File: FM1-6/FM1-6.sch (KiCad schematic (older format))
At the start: 13 parts

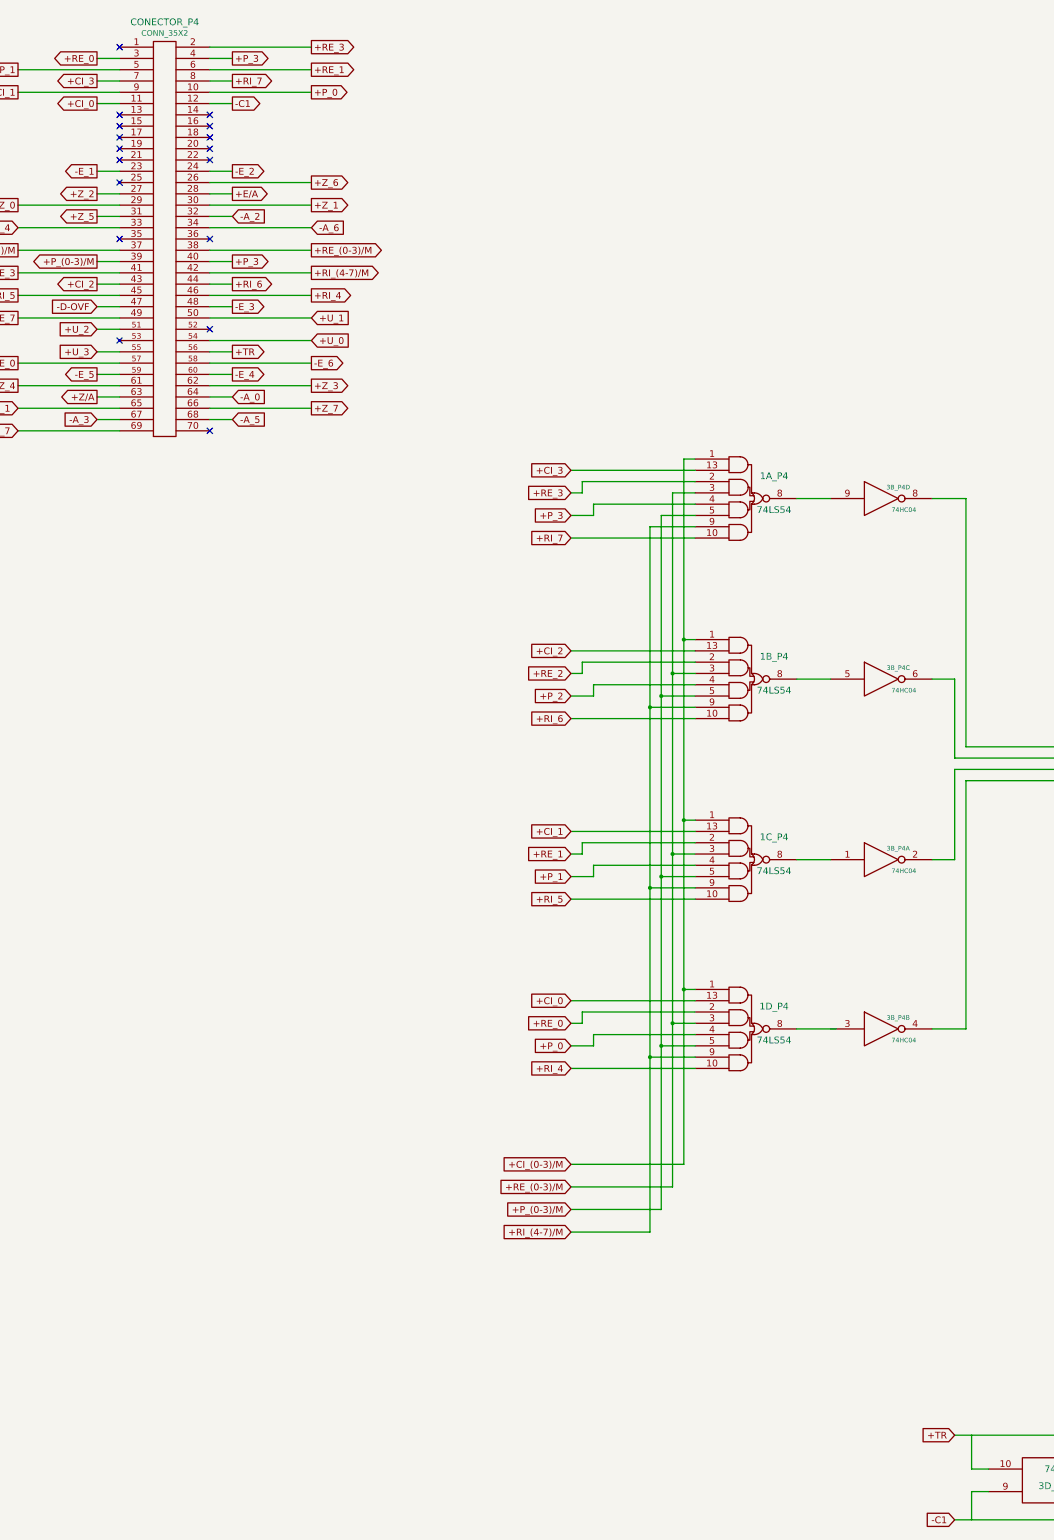
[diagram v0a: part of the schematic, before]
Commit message: criando novos projetos individuais para todas as outras pranchas que ainda faltavam serem migradas.
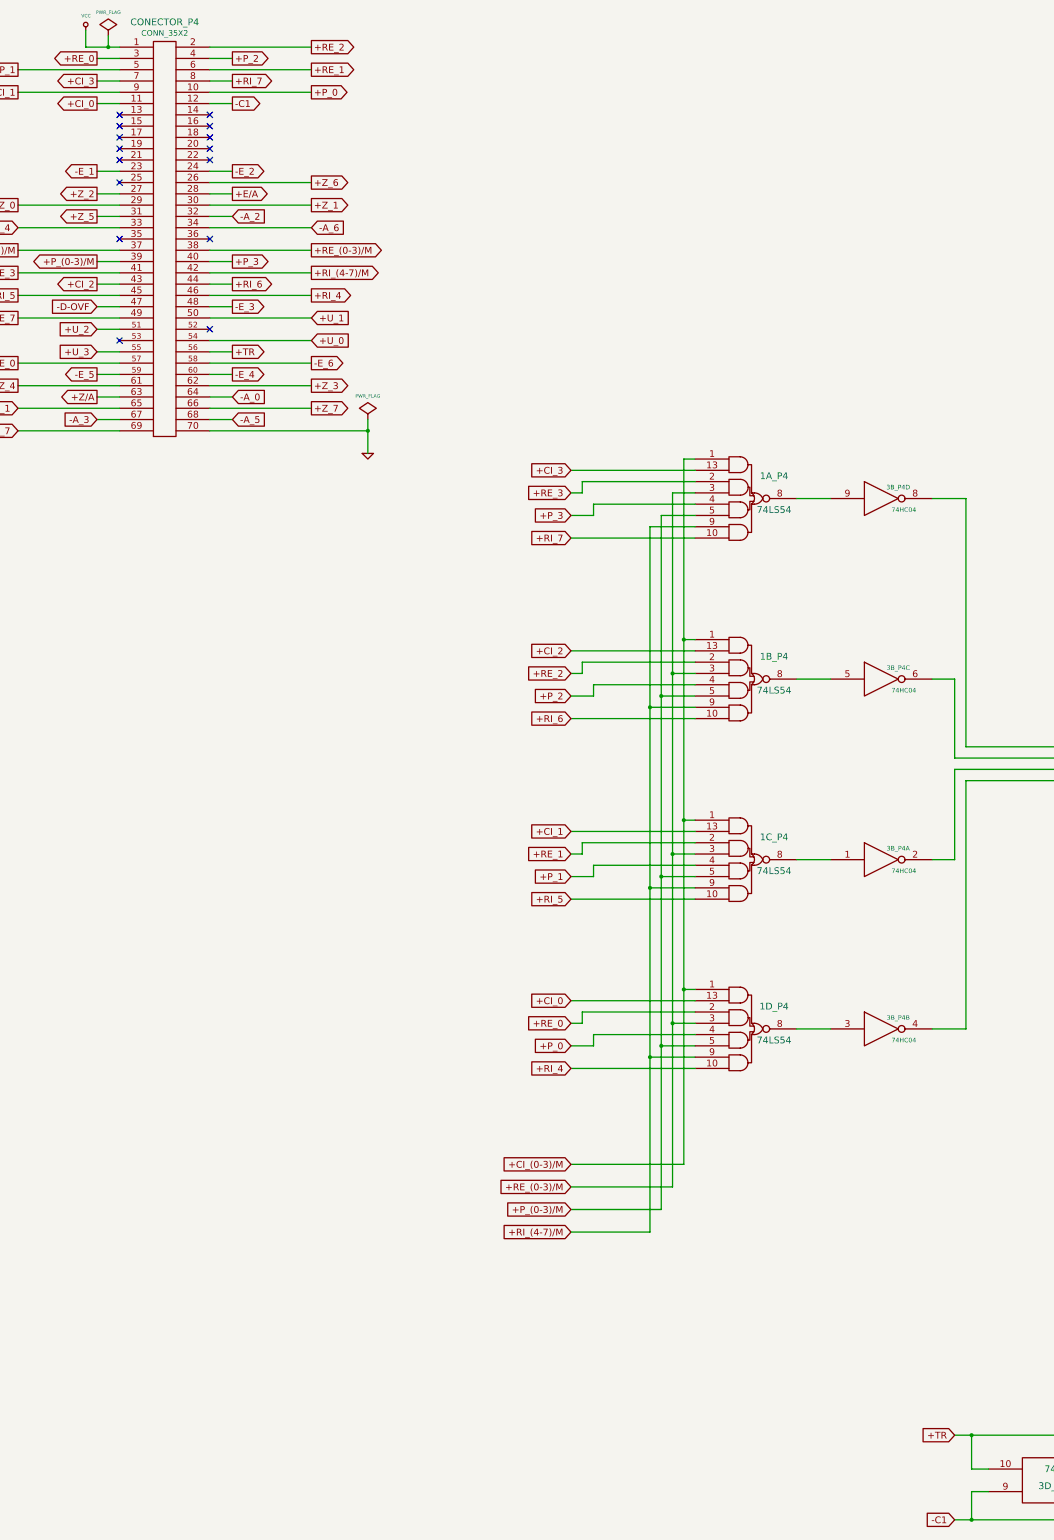
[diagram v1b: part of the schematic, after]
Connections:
- net +P_2: now also CONECTOR_P4.4 (P4)
- net +P_3: no longer CONECTOR_P4.4 (P4)
- net +RE_2: now also CONECTOR_P4.2 (P2)
- net +RE_3: no longer CONECTOR_P4.2 (P2)
- net +TR: now also 3D_P4.10
- net -C1: now also 3D_P4.9
- net GND: now also CONECTOR_P4.70 (P70)
- net VCC: now also CONECTOR_P4.1 (P1)
- net at 1D_P4.8: now also 3B_P4.3
- no-connect marks 18 -> 16
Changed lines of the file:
@@
 LIBS:memory
 LIBS:xilinx
-LIBS:special
 LIBS:microcontrollers
 LIBS:dsp
@@
 LIBS:contrib
 LIBS:valves
+LIBS:conn_35x2
 LIBS:7451
-LIBS:7454
-LIBS:7460
-LIBS:conn_35x2
-LIBS:patinhofeio-cache
 EELAYER 25 0
 EELAYER END
 $Descr A2 23386 16535
 encoding utf-8
-Sheet 13 17
+Sheet 1 1
 Title "MAIS UM E PORTA DE SELEÇÃO"
 Date "2 aug 2016"
@@
 +TR
 $Comp
-L GND #PWR055
+L GND #PWR01
 U 1 1 57728D70
 P 10500 8000
-F 0 "#PWR055" H 10500 8000 30  0001 C CNN
+F 0 "#PWR01" H 10500 8000 30  0001 C CNN
 F 1 "GND" H 10500 7930 30  0001 C CNN
 F 2 "" H 10500 8000 60  0000 C CNN
@@
 	8100 8100 8400 8100
 Wire Wire Line
-	8450 9600 8100 9600
-Wire Wire Line
 	8100 6500 8400 6500
 Wire Wire Line
@@
 	9800 13500 9650 13500
 Wire Wire Line
-	9650 13500 9650 13200
-Wire Wire Line
 	9500 13200 11300 13200
 Wire Wire Line
 	9800 13700 9650 13700
-Wire Wire Line
-	9650 13700 9650 13950
 Wire Wire Line
 	9500 13950 11300 13950
@@
 	3800 1100 2900 1100
 Text GLabel 3100 1000 2    60   Output ~ 0
-+P_3
++P_2
 Wire Wire Line
 	3100 1000 2900 1000
 Text GLabel 3800 900  2    60   Output ~ 0
-+RE_3
++RE_2
 Wire Wire Line
 	3800 900  2900 900
-NoConn ~ 2100 900
 NoConn ~ 2100 1500
 NoConn ~ 2100 1600
@@
 NoConn ~ 2900 3400
 NoConn ~ 2100 3500
-NoConn ~ 2900 4300
+$Comp
+L PWR_FLAG #FLG02
+U 1 1 587E774A
+P 4300 4200
+F 0 "#FLG02" H 4300 4295 30  0001 C CNN
+F 1 "PWR_FLAG" H 4300 4408 30  0000 C CNN
+F 2 "" H 4300 4200 60  0001 C CNN
+F 3 "" H 4300 4200 60  0001 C CNN
+	1    4300 4200
+	1    0    0    -1
+$EndComp
+$Comp
+L GND #PWR03
+U 1 1 587E77B8
+P 4300 4500
+F 0 "#PWR03" H 4300 4500 30  0001 C CNN
+F 1 "GND" H 4300 4430 30  0001 C CNN
+F 2 "" H 4300 4500 60  0001 C CNN
+F 3 "" H 4300 4500 60  0001 C CNN
+	1    4300 4500
+	1    0    0    -1
+$EndComp
+Wire Wire Line
+	4300 4200 4300 4500
+Wire Wire Line
+	2900 4300 4300 4300
+Connection ~ 4300 4300
+$Comp
+L PWR_FLAG #FLG04
+U 1 1 587E7BA4
+P 2000 800
+F 0 "#FLG04" H 2000 895 30  0001 C CNN
+F 1 "PWR_FLAG" H 2000 1008 30  0000 C CNN
+F 2 "" H 2000 800 60  0001 C CNN
+F 3 "" H 2000 800 60  0001 C CNN
+	1    2000 800
+	1    0    0    -1
+$EndComp
+$Comp
+L VCC #PWR05
+U 1 1 587E7DEB
+P 1800 750
+F 0 "#PWR05" H 1800 850 30  0001 C CNN
+F 1 "VCC" H 1803 878 30  0000 C CNN
+F 2 "" H 1800 750 60  0001 C CNN
+F 3 "" H 1800 750 60  0001 C CNN
+	1    1800 750
+	1    0    0    -1
+$EndComp
+Wire Wire Line
+	1800 900  2100 900
+Wire Wire Line
+	2000 900  2000 800
+Wire Wire Line
+	1800 900  1800 750
+Connection ~ 2000 900
+Wire Wire Line
+	8400 9600 8100 9600
+Wire Wire Line
+	9650 13500 9650 13200
+Connection ~ 9650 13200
+Wire Wire Line
+	9650 13700 9650 13950
+Connection ~ 9650 13950
 $EndSCHEMATC
